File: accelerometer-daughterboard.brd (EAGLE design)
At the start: 17.8 x 25.4 mm, 25 parts, among them Q2 BSS138, U1 LIS3DHTR, U2 AP2112K-3.3

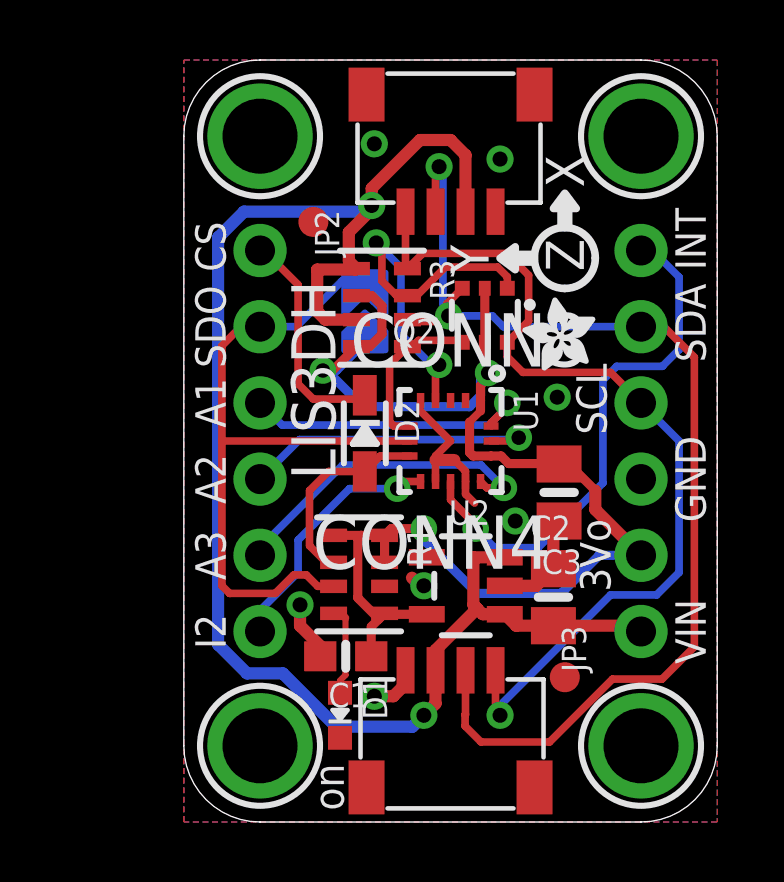
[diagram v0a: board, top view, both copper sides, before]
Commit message: Remove power supply (have 3.3 V already)
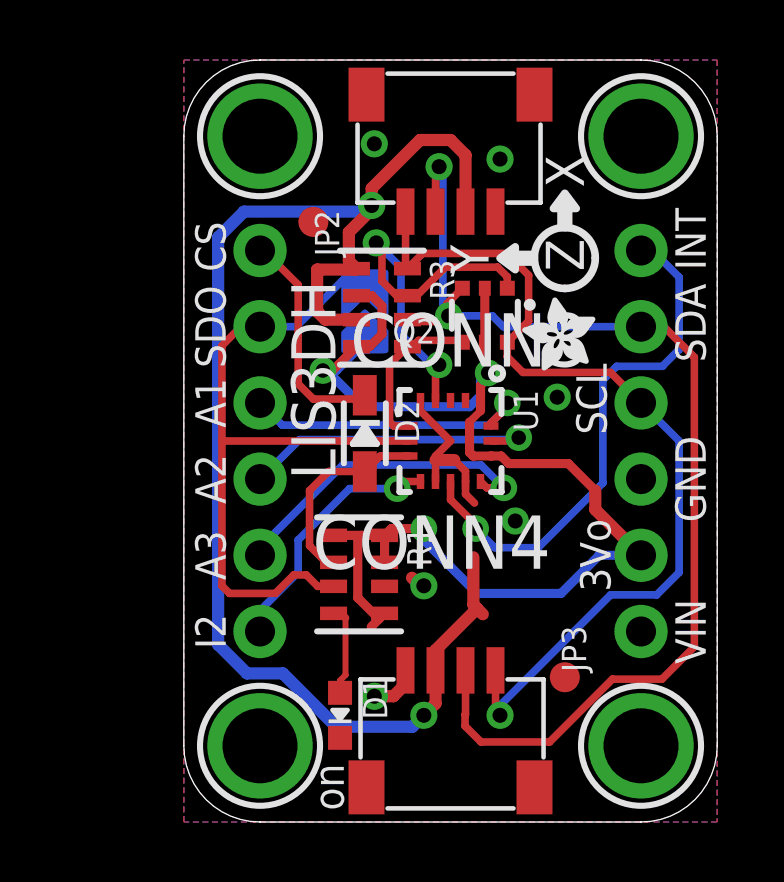
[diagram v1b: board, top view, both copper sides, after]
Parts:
- removed C1: 0.1uF, microbuilder:0603-NO
- removed C2, C3: 10uF, microbuilder:0805-NO
- removed U2: AP2112K-3.3, microbuilder:SOT23-5
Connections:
- net 3.3V: no longer C1.1, C3.1, U2.5
- net GND: no longer C1.2, C2.2, C3.2, U2.2
- net VCC: no longer C2.1, U2.1, U2.3
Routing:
- net VCC: track 53.3 -> 47.0 mm
- net GND: track 13.4 -> 7.71 mm, vias 7 -> 6
- net 3.3V: track 45.4 -> 43.1 mm

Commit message: Remove LED
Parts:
- removed D1: GREEN, microbuilder:CHIPLED_0603_NOOUTLINE
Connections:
- removed net N$1: D1.A, R1.4
- net 3.3V: no longer R1.5
- net GND: no longer D1.C
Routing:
- net N$1: track 3.03 -> 0.00 mm
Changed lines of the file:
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@@
 <element name="U$30" library="silks" package="STEMMAQT" value="" x="13.335" y="22.479" smashed="yes" rot="MR0"/>
 <element name="U$31" library="silks" package="STEMMAQT" value="" x="4.445" y="2.921" smashed="yes" rot="MR180"/>
-<element name="D1" library="microbuilder" package="CHIPLED_0603_NOOUTLINE" value="GREEN" x="5.207" y="3.556" smashed="yes" rot="R180">
-<attribute name="NAME" x="5.969" y="4.826" size="0.8128" layer="25" ratio="18" rot="R270"/>
-<attribute name="VALUE" x="4.318" y="2.032" size="1.016" layer="27" ratio="10" rot="R270"/>
-</element>
 <element name="U1" library="microbuilder" package="LGA16_3X3MM" value="LIS3DHTR" x="8.89" y="12.7" smashed="yes" rot="R270">
 <attribute name="NAME" x="10.99" y="14.4" size="0.8128" layer="25" ratio="18" rot="R270"/>
@@
 <via x="6.35" y="4.191" extent="1-16" drill="0.5"/>
 <via x="10.541" y="22.098" extent="1-16" drill="0.5"/>
-<contactref element="D1" pad="C"/>
 <wire x1="7.39" y1="5.054" x2="7.34" y2="5.004" width="0.4064" layer="1"/>
 <wire x1="7.34" y1="5.004" x2="7.34" y2="4.546" width="0.4064" layer="1"/>
@@
 <wire x1="6.692" y1="7.855" x2="7.6054" y2="8.1426" width="0" layer="19" extent="1-1"/>
 <wire x1="7.39" y1="5.054" x2="7.874" y2="7.874" width="0" layer="19" extent="1-1"/>
-<wire x1="5.207" y1="2.806" x2="6.35" y2="4.191" width="0" layer="19" extent="1-1"/>
 </signal>
 <signal name="SDA">
@@
 <wire x1="15.24" y1="8.89" x2="13.716" y2="10.414" width="0.4064" layer="1"/>
 <wire x1="13.716" y1="10.414" x2="13.716" y2="11.049" width="0.4064" layer="1"/>
-<contactref element="R1" pad="5"/>
 <contactref element="R1" pad="7"/>
 <wire x1="5.754" y1="15.845" x2="4.797" y2="14.888" width="0.3048" layer="1"/>
@@
 <wire x1="5.08" y1="15.0495" x2="4.6355" y2="15.0495" width="0.3048" layer="16"/>
 <wire x1="6.2475" y1="6.5105" x2="6.50425" y2="6.76725" width="0.3048" layer="1"/>
-<wire x1="6.50425" y1="6.76725" x2="6.692" y2="6.955" width="0.3048" layer="1"/>
-<wire x1="6.723" y1="6.924" x2="6.692" y2="6.955" width="0.3048" layer="1"/>
 <wire x1="6.692" y1="9.555" x2="5.9055" y2="9.555" width="0.3048" layer="1"/>
 <wire x1="5.9055" y1="9.555" x2="4.992" y2="9.555" width="0.3048" layer="1"/>
@@
 <wire x1="9.967" y1="6.924" x2="15.047" y2="6.543" width="0" layer="19" extent="1-1"/>
 </signal>
-<signal name="N$1">
-<contactref element="D1" pad="A"/>
-<contactref element="R1" pad="4"/>
-<wire x1="5.207" y1="4.306" x2="5.207" y2="4.71545" width="0.2032" layer="1"/>
-<wire x1="5.207" y1="4.71545" x2="5.3898" y2="4.89825" width="0.2032" layer="1"/>
-<wire x1="5.3898" y1="6.8022" x2="5.3898" y2="4.89825" width="0.2032" layer="1"/>
-<wire x1="4.992" y1="6.955" x2="5.237" y2="6.955" width="0.254" layer="1"/>
-<wire x1="5.237" y1="6.955" x2="5.3898" y2="6.8022" width="0.254" layer="1"/>
-</signal>
 <signal name="CS">

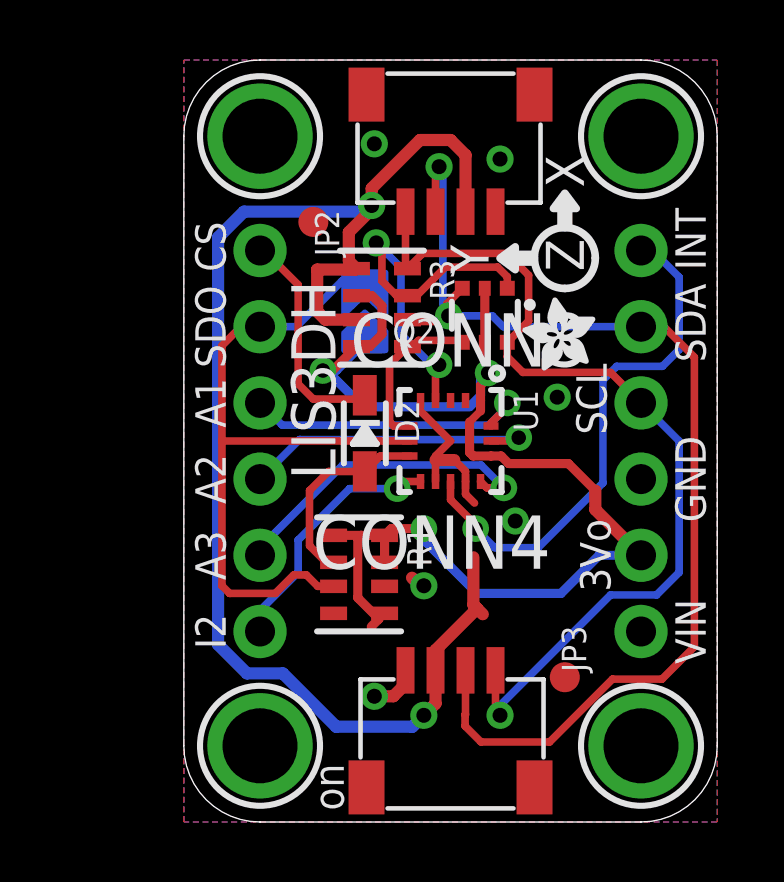
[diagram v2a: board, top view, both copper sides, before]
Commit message: Remove I2C level-shifting
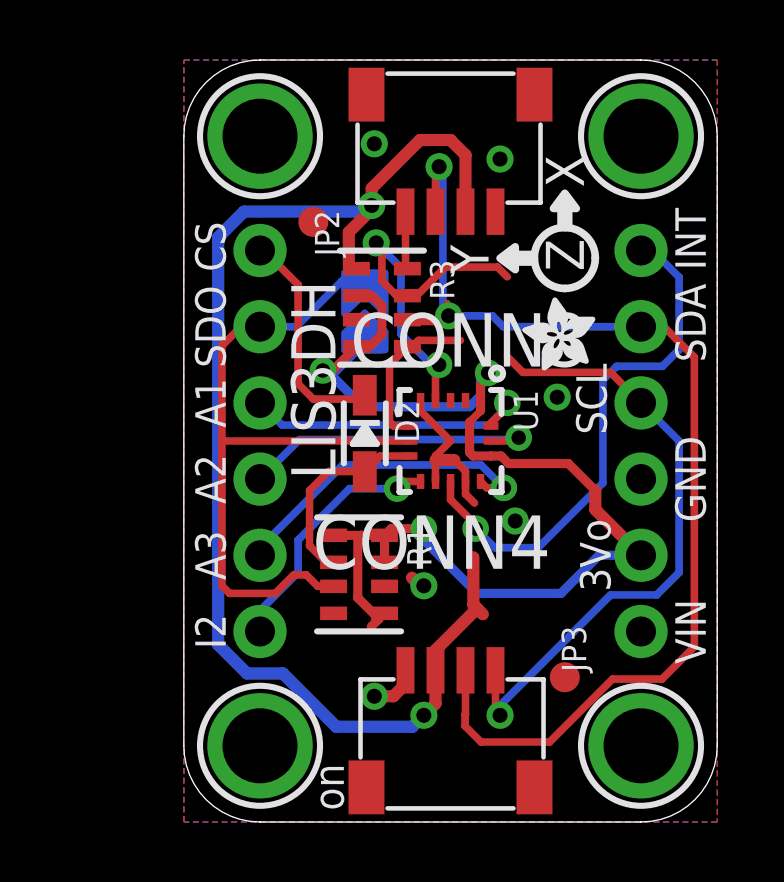
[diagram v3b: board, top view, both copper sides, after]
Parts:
- removed Q2: BSS138, microbuilder:SOT363
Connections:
- net 3.3V: no longer Q2.2, Q2.5
- net SCL: no longer Q2.6, R3.8
- net SCL_3V: no longer Q2.1
- net SDA: no longer Q2.3, R3.6
- net SDA_3V: no longer Q2.4
- net VCC: no longer R3.1, R3.3
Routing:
- net SCL: track 30.5 -> 22.8 mm
- net VCC: track 47.0 -> 42.5 mm
- net 3.3V: track 42.8 -> 40.1 mm
- net SDA: track 38.7 -> 37.9 mm
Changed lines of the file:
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@@
 <attribute name="VALUE" x="5.194" y="17.8945" size="1.016" layer="27" font="vector" ratio="10" rot="R90"/>
-</element>
-<element name="Q2" library="microbuilder" package="SOT363" value="BSS138" x="10.033" y="16.891" smashed="yes" rot="R180">
-<attribute name="NAME" x="8.382" y="16.764" size="0.8128" layer="25" ratio="18" rot="R180"/>
-<attribute name="VALUE" x="13.462" y="19.6215" size="1.016" layer="27" ratio="10" rot="R180"/>
 </element>
 <element name="U$1" library="microbuilder" package="MOUNTINGHOLE_2.5_PLATED" value="MOUNTINGHOLE2.5" x="2.54" y="2.54" smashed="yes" rot="R90">
@@
 </signal>
 <signal name="SDA">
-<contactref element="Q2" pad="3"/>
-<contactref element="R3" pad="6"/>
 <contactref element="CONN4" pad="3"/>
 <contactref element="CONN3" pad="3"/>
 <wire x1="8.7875" y1="16.872" x2="8.597" y2="16.6815" width="0.254" layer="1"/>
-<wire x1="7.454" y1="16.745" x2="7.5175" y2="16.6815" width="0.254" layer="1"/>
 <wire x1="7.5175" y1="16.6815" x2="8.597" y2="16.6815" width="0.254" layer="1"/>
 <wire x1="8.7875" y1="16.872" x2="8.8265" y2="16.872" width="0.254" layer="1"/>
 <wire x1="8.8265" y1="16.872" x2="8.775" y2="16.9235" width="0.254" layer="1"/>
 <wire x1="8.775" y1="17.283" x2="8.775" y2="16.9235" width="0.254" layer="1"/>
-<wire x1="8.775" y1="17.283" x2="9.283" y2="17.791" width="0.254" layer="1"/>
 <wire x1="9.39" y1="5.054" x2="9.39" y2="3.57860625" width="0.254" layer="1"/>
 <wire x1="9.39" y1="3.57860625" x2="9.37539375" y2="3.57860625" width="0.254" layer="1"/>
@@
 </signal>
 <signal name="SCL">
-<contactref element="Q2" pad="6"/>
-<contactref element="R3" pad="8"/>
 <contactref element="CONN4" pad="4"/>
 <contactref element="CONN3" pad="4"/>
 <wire x1="7.39" y1="20.346" x2="7.39" y2="18.509" width="0.254" layer="1"/>
-<wire x1="7.39" y1="18.509" x2="7.454" y2="18.445" width="0.254" layer="1"/>
 <wire x1="10.39" y1="5.054" x2="10.39" y2="3.707" width="0.254" layer="1"/>
 <wire x1="10.39" y1="3.707" x2="10.541" y2="3.556" width="0.254" layer="1"/>
 <via x="10.541" y="3.556" extent="1-16" drill="0.5"/>
-<wire x1="10.783" y1="15.991" x2="10.7835" y2="15.9905" width="0.254" layer="1"/>
-<wire x1="10.783" y1="15.991" x2="10.783" y2="15.506" width="0.254" layer="1"/>
 <wire x1="10.783" y1="15.506" x2="11.303" y2="14.986" width="0.254" layer="1"/>
 <wire x1="11.303" y1="14.986" x2="14.224" y2="14.986" width="0.254" layer="1"/>
-<wire x1="7.454" y1="18.445" x2="7.962" y2="18.953" width="0.254" layer="1"/>
-<wire x1="7.962" y1="18.953" x2="10.765" y2="18.953" width="0.254" layer="1"/>
-<wire x1="10.765" y1="18.953" x2="11.4935" y2="18.2245" width="0.254" layer="1"/>
-<wire x1="11.4935" y1="18.2245" x2="11.4935" y2="16.7005" width="0.254" layer="1"/>
-<wire x1="11.4935" y1="16.7005" x2="10.7835" y2="15.9905" width="0.254" layer="1"/>
 <contactref element="JP3" pad="4"/>
 <wire x1="14.224" y1="14.986" x2="15.24" y2="13.97" width="0.254" layer="1"/>
@@
 <wire x1="15.7607" y1="7.5692" x2="16.51" y2="8.3185" width="0.254" layer="16"/>
 <wire x1="16.51" y1="8.3185" x2="16.51" y2="12.7" width="0.254" layer="16"/>
+<wire x1="10.783" y1="15.506" x2="7.39" y2="18.509" width="0" layer="19" extent="1-1"/>
 </signal>
 <signal name="SCL_3V">
 <contactref element="R3" pad="7"/>
-<contactref element="Q2" pad="1"/>
 <wire x1="7.454" y1="17.545" x2="7.093" y2="17.545" width="0.254" layer="1"/>
 <wire x1="6.604" y1="19.1135" x2="6.604" y2="18.034" width="0.254" layer="1"/>
@@
 <wire x1="7.766" y1="17.545" x2="8.7168" y2="18.4958" width="0.254" layer="1"/>
 <wire x1="10.4592" y1="18.4958" x2="10.783" y2="18.172" width="0.254" layer="1"/>
-<wire x1="10.783" y1="18.172" x2="10.783" y2="17.791" width="0.254" layer="1"/>
 <contactref element="U1" pad="4"/>
 <via x="8.509" y="15.24" extent="1-16" drill="0.4826"/>
@@
 <signal name="SDA_3V">
 <contactref element="R3" pad="5"/>
-<contactref element="Q2" pad="4"/>
 <wire x1="7.8225" y1="16.0545" x2="9.2195" y2="16.0545" width="0.254" layer="1"/>
-<wire x1="9.283" y1="15.991" x2="9.2195" y2="16.0545" width="0.254" layer="1"/>
 <wire x1="7.8225" y1="16.0545" x2="7.613" y2="15.845" width="0.254" layer="1"/>
 <wire x1="7.613" y1="15.845" x2="7.454" y2="15.845" width="0.254" layer="1"/>
@@
 <signal name="3.3V" class="2">
 <contactref element="R3" pad="4"/>
-<contactref element="Q2" pad="2"/>
 <contactref element="R3" pad="2"/>
-<contactref element="Q2" pad="5"/>
 <wire x1="5.754" y1="17.545" x2="6.2675" y2="17.545" width="0.3048" layer="1"/>
 <wire x1="6.2675" y1="17.545" x2="6.604" y2="17.2085" width="0.3048" layer="1"/>
@@
 <wire x1="13.843" y1="8.89" x2="15.24" y2="8.89" width="0.3048" layer="16"/>
 <wire x1="13.843" y1="8.89" x2="12.573" y2="7.62" width="0.3048" layer="16"/>
-<wire x1="10.033" y1="15.991" x2="10.033" y2="15.081" width="0.3048" layer="1"/>
 <wire x1="10.144" y1="14.97" x2="10.033" y2="15.081" width="0.3048" layer="1"/>
-<wire x1="10.033" y1="15.991" x2="10.033" y2="17.791" width="0.3048" layer="1"/>
 <wire x1="10.24" y1="12.2" x2="10.57919375" y2="12.2" width="0.3048" layer="1"/>
 <wire x1="10.57919375" y1="12.2" x2="10.8318875" y2="11.94730625" width="0.3048" layer="1"/>
@@
 <contactref element="CONN3" pad="2"/>
 <contactref element="CONN4" pad="2"/>
-<contactref element="R3" pad="1"/>
-<contactref element="R3" pad="3"/>
-<wire x1="5.754" y1="16.745" x2="4.718" y2="16.745" width="0.4064" layer="1"/>
-<wire x1="4.445" y1="17.018" x2="4.445" y2="18.415" width="0.4064" layer="1"/>
-<wire x1="4.718" y1="16.745" x2="4.445" y2="17.018" width="0.4064" layer="1"/>
 <wire x1="9.652" y1="8.824" x2="9.652" y2="7.239" width="0.4064" layer="1"/>
 <wire x1="9.652" y1="7.239" x2="9.7765" y2="7.1145" width="0.4064" layer="1"/>
@@
 <wire x1="8.39" y1="5.054" x2="8.39" y2="5.728" width="0.4064" layer="1"/>
 <wire x1="8.39" y1="5.728" x2="9.7765" y2="7.1145" width="0.4064" layer="1"/>
-<wire x1="4.445" y1="18.415" x2="5.724" y2="18.415" width="0.4064" layer="1"/>
-<wire x1="5.724" y1="18.415" x2="5.754" y2="18.445" width="0.4064" layer="1"/>
 <wire x1="9.39" y1="20.346" x2="9.39" y2="22.233" width="0.4064" layer="1"/>
 <wire x1="9.39" y1="22.233" x2="8.89" y2="22.733" width="0.4064" layer="1"/>
@@
 <wire x1="6.262" y1="20.4225" x2="5.5" y2="19.6605" width="0.4064" layer="1"/>
 <wire x1="5.5" y1="19.6605" x2="5.5" y2="18.699" width="0.4064" layer="1"/>
-<wire x1="5.754" y1="18.445" x2="5.5" y2="18.699" width="0.4064" layer="1"/>
 <wire x1="2.003425" y1="20.3454" x2="6.0579" y2="20.3454" width="0.4064" layer="16"/>
 <wire x1="6.262" y1="20.5495" x2="6.0579" y2="20.3454" width="0.4064" layer="16"/>
